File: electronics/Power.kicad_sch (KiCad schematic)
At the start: 18 parts, among them J4 Conn_01x02_Socket, Q1 IRLML6401, U3 LM1117DT-ADJ, U4 AOZ1280CI

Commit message: Ordered this version.
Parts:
- removed C16: 10u, Capacitor_SMD:C_0805_2012Metric, symbol Device:C
- removed J4: Conn_01x02_Socket, Connector_JST:JST_PH_S2B-PH-K_1x02_P2.00mm_Horizontal, symbol Connector:Conn_01x02_Socket
- removed U3: LM1117DT-ADJ, Package_TO_SOT_SMD:SOT-223-3_TabPin2, symbol Regulator_Linear:LM1117DT-ADJ
- added C15, C27, C28: 4.7u, Capacitor_SMD:C_0603_1608Metric, symbol Device:C
- added R14: 4.09k, Resistor_SMD:R_0402_1005Metric, symbol Device:R
- added R15: 1k, Resistor_SMD:R_0402_1005Metric, symbol Device:R
- added TP8: TestPoint, TestPoint:TestPoint_Pad_D1.0mm, symbol Connector:TestPoint
- added U3, U5: TLV75801PDRV, Package_SON:WSON-6-1EP_2x2mm_P0.65mm_EP1x1.6mm, symbol Regulator_Linear:TLV75801PDRV
- C16: renamed from C18; footprint Capacitor_SMD:C_0805_2012Metric -> Capacitor_SMD:C_0603_1608Metric
- C17: value 10u -> 4.7u; footprint Capacitor_SMD:C_0805_2012Metric -> Capacitor_SMD:C_0603_1608Metric; Digikey 490-5523-1-ND -> (none); JLCPCB C96446 -> C1705
- C20: renamed from C22; footprint Capacitor_SMD:C_0805_2012Metric -> Capacitor_SMD:C_0603_1608Metric
- L1: footprint Inductor_SMD:L_Taiyo-Yuden_MD-3030 -> Inductor_SMD:L_1210_3225Metric
- R10: renamed from R12; value 1k -> 5k; JLCPCB (none) -> C5948099
- R11: value 1.6k -> 1k; JLCPCB C102825 -> C11702
- R12: renamed from R15; footprint Resistor_SMD:R_0603_1608Metric -> Resistor_SMD:R_0402_1005Metric; JLCPCB (none) -> C2906873
- R13: renamed from R16; footprint Resistor_SMD:R_0603_1608Metric -> Resistor_SMD:R_0402_1005Metric; JLCPCB (none) -> C295883
- renumbered C20 to C18, TP1 to TP6, TP3 to TP7
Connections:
- net 3V3: now also C28.1, U3.1 (OUT); no longer C17.1
- net GND: now also C15.2, C27.2, C28.2, R15.2, U3.3 (GND), U3.7 (GND), U5.3 (GND), U5.7 (GND)
- net VCC: now also C15.1, C27.1, U3.4 (EN), U3.6 (IN), U5.4 (EN), U5.6 (IN)
- net PRE_OUT: now reaches C20.1, D5.2 (A), L1.2, R12.1
- net LX: now reaches C18.2, D4.1 (K), L1.1, U4.6 (LX)
- net at R10.2, R11.1: now also U3.2 (FB)
- new net: R14.2, R15.1, U5.2 (FB)
- new net 2V8: C17.1, R14.1, TP8.1, U5.1 (OUT)
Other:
- moved on the sheet: C16, C18, C20, D4, D5, L1, Q1, R10, R11, R12, R13, TP6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

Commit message: Major refactor to rev B
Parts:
- removed TP6, TP7, TP8: TestPoint, TestPoint:TestPoint_Pad_D1.0mm, symbol Connector:TestPoint
- added TP2, TP3, TP4: TestPoint, TestPoint:TestPoint_Pad_D1.0mm, symbol Connector:TestPoint
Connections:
- net 2V8: now also TP4.1
- net 3V3: now also TP3.1
- net VCC: now also TP2.1

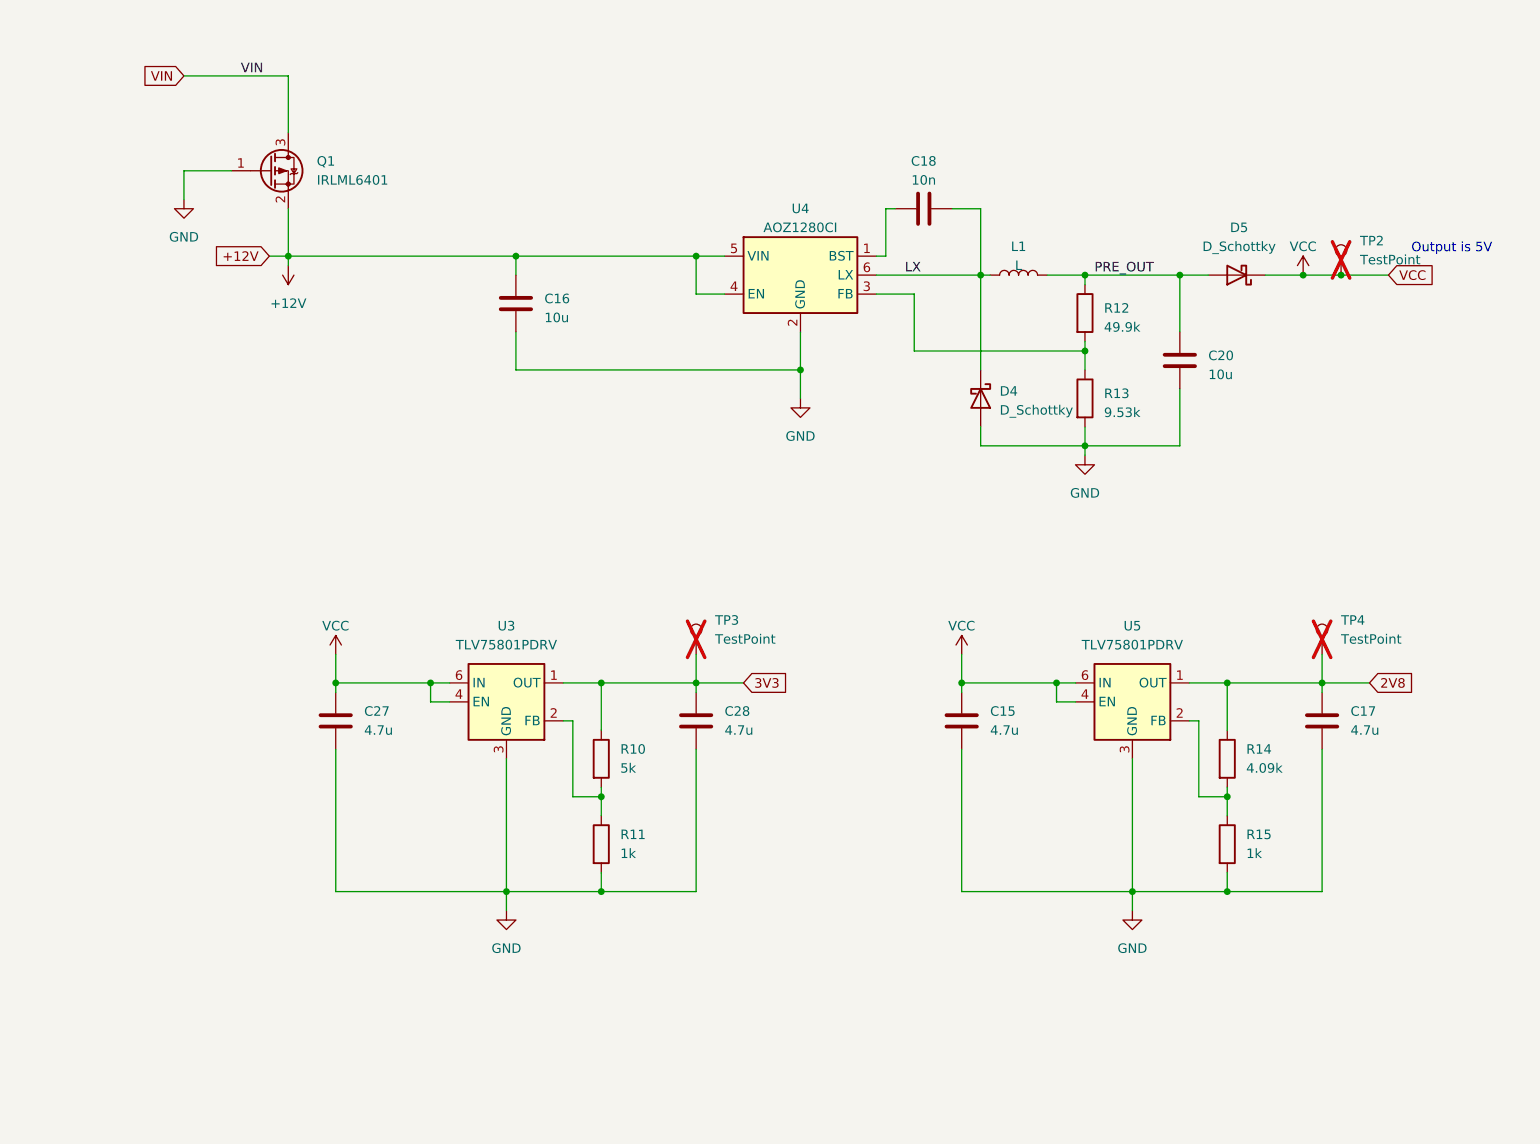
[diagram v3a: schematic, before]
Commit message: Refactored the design to use basic parts.
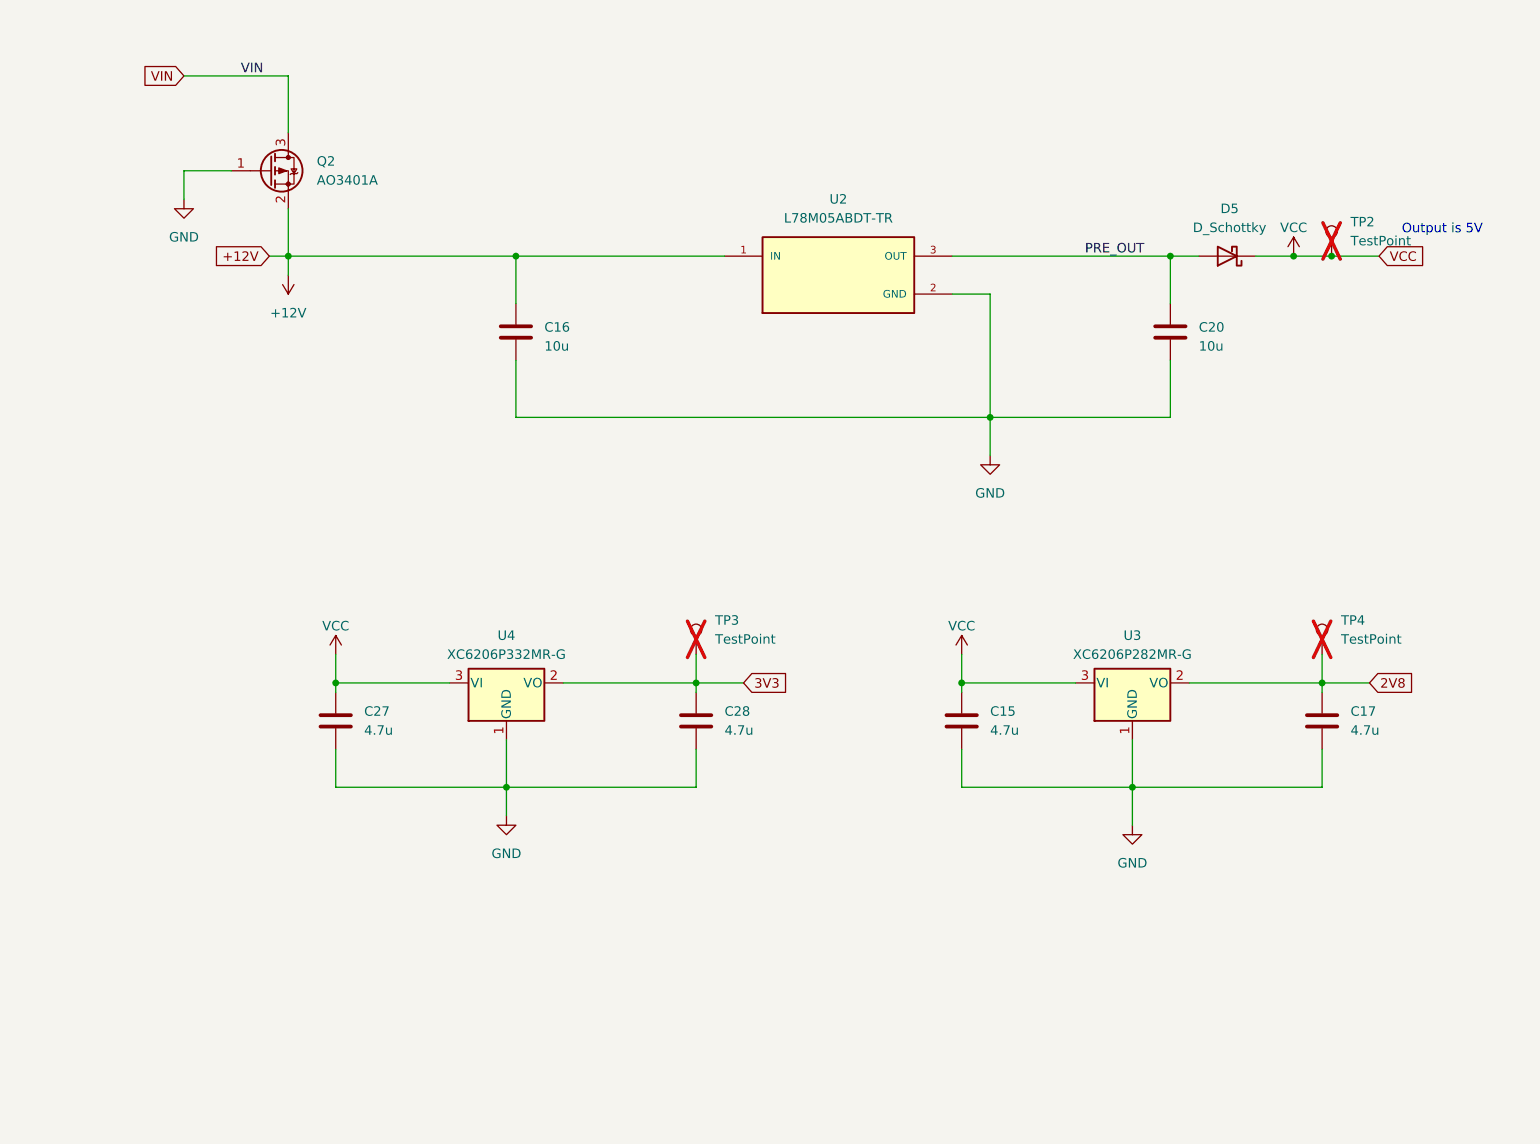
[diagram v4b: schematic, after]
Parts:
- removed C18: 10n, Capacitor_SMD:C_0603_1608Metric, symbol Device:C
- removed D4: D_Schottky, Diode_SMD:D_SOD-123, symbol Device:D_Schottky
- removed L1: L, Inductor_SMD:L_1210_3225Metric, symbol Device:L
- removed Q1: IRLML6401, Package_TO_SOT_SMD:SOT-23, symbol Transistor_FET:IRLML6401
- removed R10: 5k, Resistor_SMD:R_0402_1005Metric, symbol Device:R
- removed R11, R15: 1k, Resistor_SMD:R_0402_1005Metric, symbol Device:R
- removed R12: 49.9k, Resistor_SMD:R_0402_1005Metric, symbol Device:R
- removed R13: 9.53k, Resistor_SMD:R_0402_1005Metric, symbol Device:R
- removed R14: 4.09k, Resistor_SMD:R_0402_1005Metric, symbol Device:R
- removed U3, U5: TLV75801PDRV, Package_SON:WSON-6-1EP_2x2mm_P0.65mm_EP1x1.6mm, symbol Regulator_Linear:TLV75801PDRV
- removed U4: AOZ1280CI, Package_TO_SOT_SMD:SOT-23-6, symbol Regulator_Switching:AOZ1280CI
- added Q2: AO3401A, Package_TO_SOT_SMD:SOT-23, symbol Transistor_FET:AO3401A
- added U2: L78M05ABDT-TR, footprints:VREG_L78M05ABDT-TR, symbol General:L78M05ABDT-TR
- added U3: XC6206P282MR-G, Package_TO_SOT_SMD:SOT-23, symbol Regulator_Linear:TPS7A0508PDBZ
- added U4: XC6206P332MR-G, Package_TO_SOT_SMD:SOT-23, symbol Regulator_Linear:TPS7A0508PDBZ
- C15, C17, C27, C28: JLCPCB C1705 -> C19666
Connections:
- net +12V: now also Q2.2 (S), U2.1 (IN)
- net 2V8: now also U3.2 (VO)
- net 3V3: now also U4.2 (VO)
- net GND: now also Q2.1 (G), U2.2 (GND), U3.1 (GND), U4.1 (GND)
- net PRE_OUT: now also U2.3 (OUT)
- net VCC: now also U3.3 (VI), U4.3 (VI)
- net VIN: now also Q2.3 (D)
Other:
- moved on the sheet: C16, C20, D5, TP2

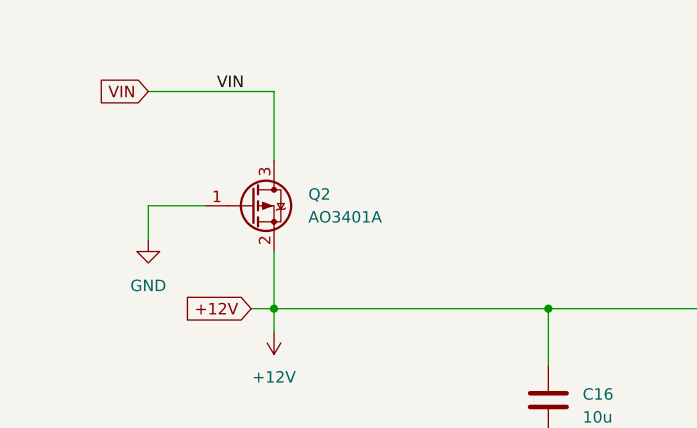
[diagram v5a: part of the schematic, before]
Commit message: Updated to the latest STM32CubeMX and now using STM32CubeIDE for VS Code.
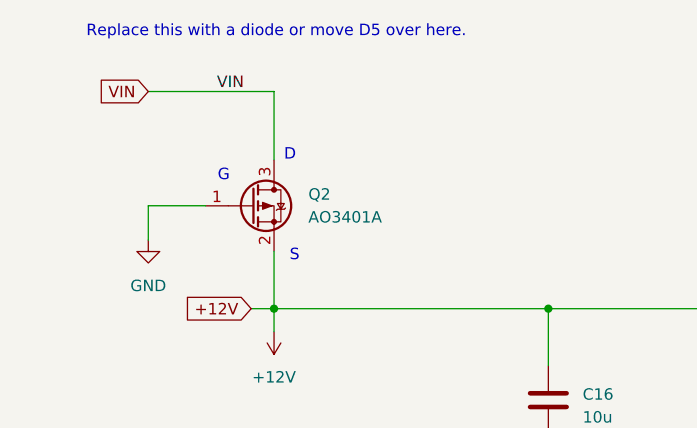
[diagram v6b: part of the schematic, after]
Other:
- note added: "D"
- note added: "G"
- note added: "Replace this with a diode or move D5 over here."
- note added: "S"
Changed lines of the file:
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@@
 	(generator_version "9.0")
 	(paper "A4")
+	(text "D"
+		(exclude_from_sim no)
+		(at 83.058 35.052 0)
+		(effects
+			(font
+				(size 1.27 1.27)
+			)
+		)
+	)
+	(text "G"
+		(exclude_from_sim no)
+		(at 75.692 37.338 0)
+		(effects
+			(font
+				(size 1.27 1.27)
+			)
+		)
+	)
 	(text "Output is 5V"
 		(exclude_from_sim no)
@@
 		)
 	)
+	(text "Replace this with a diode or move D5 over here."
+		(exclude_from_sim no)
+		(at 81.534 21.336 0)
+		(effects
+			(font
+				(size 1.27 1.27)
+			)
+		)
+	)
+	(text "S"
+		(exclude_from_sim no)
+		(at 83.566 46.228 0)
+		(effects
+			(font
+				(size 1.27 1.27)
+			)
+		)
+	)
